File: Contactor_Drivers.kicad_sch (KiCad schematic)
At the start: 33 parts, among them Con1 LED, Con2 LED, Con3 LED, J4 Conn_01x04, J5 Conn_01x04, J6 Conn_01x04, J7 Conn_01x04, Q4 IRLML0030, Q5 IRLML0030, Q6 IRLML0030, U8 VOS618A

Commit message: changed some res values
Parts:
- R21, R23, R25: value 1k -> 2k
- R26: value R_US -> 1k
- U8: value VOS618A -> TCMT1106
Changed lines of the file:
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@@
 			)
 		)
-		(property "Value" "1k"
+		(property "Value" "2k"
 			(at 127 36.83 90)
 			(effects
@@
 			)
 		)
-		(property "Value" "R_US"
+		(property "Value" "1k"
 			(at 59.69 171.45 90)
 			(effects
@@
 			)
 		)
-		(property "Value" "1k"
+		(property "Value" "2k"
 			(at 57.15 36.83 90)
 			(effects
@@
 			)
 		)
-		(property "Value" "VOS618A"
+		(property "Value" "TCMT1106"
 			(at 77.47 171.45 0)
 			(effects
@@
 			)
 		)
-		(property "Value" "1k"
+		(property "Value" "2k"
 			(at 236.22 36.83 90)
 			(effects

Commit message: new revision for frank review
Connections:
- net M_Sense: no longer R26.1
- net MSense: now reaches C20.1, J6.2 (Pin_2), R32.2
- net MSense: now also R26.1
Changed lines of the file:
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@@
+	(wire
+		(pts
+			(xy 67.31 100.33) (xy 67.31 102.87)
+		)
+		(stroke
+			(width 0)
+			(type default)
+		)
+	)
 	(wire
 		(pts
@@
 	(wire
 		(pts
+			(xy 64.77 105.41) (xy 69.85 105.41)
+		)
+		(stroke
+			(width 0)
+			(type default)
+		)
+	)
+	(wire
+		(pts
 			(xy 241.3 102.87) (xy 248.92 102.87)
 		)
@@
 	(wire
 		(pts
+			(xy 44.45 175.26) (xy 55.88 175.26)
+		)
+		(stroke
+			(width 0)
+			(type default)
+		)
+	)
+	(wire
+		(pts
 			(xy 128.27 107.95) (xy 128.27 111.76)
 		)
@@
 	(wire
 		(pts
-			(xy 62.23 102.87) (xy 69.85 102.87)
+			(xy 62.23 100.33) (xy 67.31 100.33)
 		)
 		(stroke
@@
 	(wire
 		(pts
+			(xy 67.31 102.87) (xy 69.85 102.87)
+		)
+		(stroke
+			(width 0)
+			(type default)
+		)
+	)
+	(wire
+		(pts
 			(xy 219.71 107.95) (xy 222.25 107.95)
 		)
@@
 	(wire
 		(pts
-			(xy 48.26 175.26) (xy 55.88 175.26)
-		)
-		(stroke
-			(width 0)
-			(type default)
-		)
-	)
-	(wire
-		(pts
 			(xy 119.38 50.8) (xy 119.38 54.61)
 		)
@@
 	(wire
 		(pts
+			(xy 64.77 102.87) (xy 64.77 105.41)
+		)
+		(stroke
+			(width 0)
+			(type default)
+		)
+	)
+	(wire
+		(pts
 			(xy 66.04 71.12) (xy 66.04 77.47)
 		)
@@
 	(wire
 		(pts
-			(xy 69.85 105.41) (xy 62.23 105.41)
+			(xy 64.77 102.87) (xy 62.23 102.87)
 		)
 		(stroke
@@
 	(text "Motor\nCoil+"
 		(exclude_from_sim no)
-		(at 65.278 98.806 0)
+		(at 72.39 98.044 0)
 		(effects
 			(font
@@
 		)
 	)
+	(label "MSense"
+		(at 44.45 175.26 0)
+		(fields_autoplaced yes)
+		(effects
+			(font
+				(size 1.27 1.27)
+			)
+			(justify left bottom)
+		)
+	)
 	(label "MCon-"
 		(at 80.01 54.61 180)
@@
 			)
 			(justify right bottom)
+		)
+	)
+	(label "MSense"
+		(at 62.23 107.95 0)
+		(fields_autoplaced yes)
+		(effects
+			(font
+				(size 1.27 1.27)
+			)
+			(justify left bottom)
 		)
 	)
@@
 	(hierarchical_label "LV+"
 		(shape input)
-		(at 62.23 105.41 180)
+		(at 62.23 102.87 180)
 		(fields_autoplaced yes)
 		(effects
@@
 	(hierarchical_label "LV+"
 		(shape input)
-		(at 62.23 102.87 180)
+		(at 62.23 100.33 180)
 		(fields_autoplaced yes)
 		(effects
@@
 		)
 	)
-	(hierarchical_label "M_Sense"
-		(shape output)
-		(at 48.26 175.26 180)
-		(fields_autoplaced yes)
-		(effects
-			(font
-				(size 1.27 1.27)
-			)
-			(justify right)
-		)
-	)

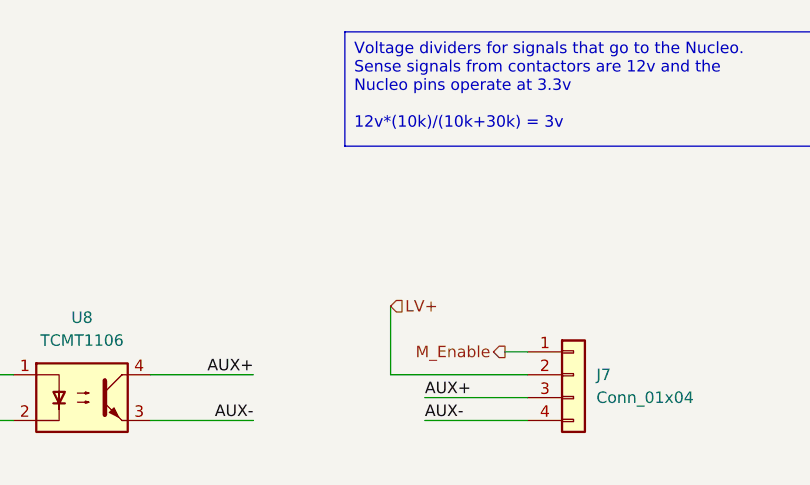
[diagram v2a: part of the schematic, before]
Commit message: emergency m_enable fix
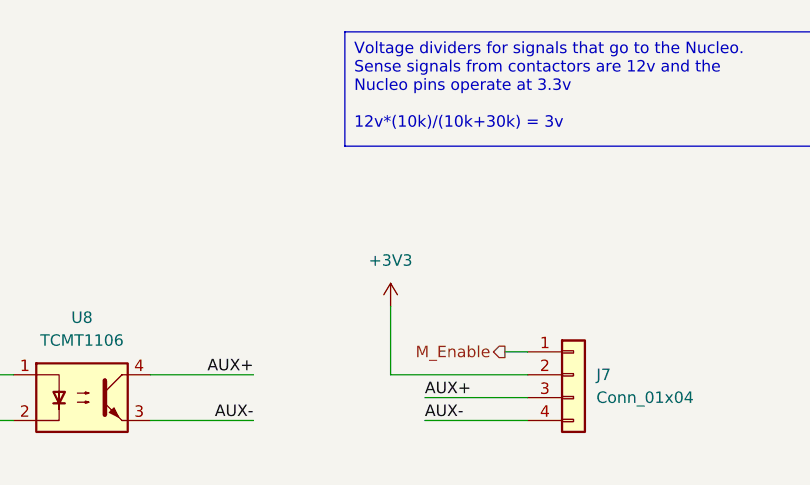
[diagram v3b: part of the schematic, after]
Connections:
- net LV+: no longer J7.2 (Pin_2)
- new net +3V3: J7.2 (Pin_2)
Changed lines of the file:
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@@
-		)
-	)
-	(hierarchical_label "LV+"
-		(shape input)
-		(at 111.76 167.64 0)
-		(fields_autoplaced yes)
-		(effects
-			(font
-				(size 1.27 1.27)
-			)
-			(justify left)
 		)
 	)
@@
 					(unit 1)
 				)
+			)
+		)
+	)
+	(symbol
+		(lib_id "power:+3V3")
+		(at 111.76 167.64 0)
+		(unit 1)
+		(exclude_from_sim no)
+		(in_bom yes)
+		(on_board yes)
+		(dnp no)
+		(fields_autoplaced yes)
+		(property "Reference" "#PWR018"
+			(at 111.76 171.45 0)
+			(effects
+				(font
+					(size 1.27 1.27)
+				)
+				(hide yes)
+			)
+		)
+		(property "Value" "+3V3"
+			(at 111.76 162.56 0)
+			(effects
+				(font
+					(size 1.27 1.27)
+				)
+			)
+		)
+		(property "Footprint" ""
+			(at 111.76 167.64 0)
+			(effects
+				(font
+					(size 1.27 1.27)
+				)
+				(hide yes)
+			)
+		)
+		(property "Datasheet" ""
+			(at 111.76 167.64 0)
+			(effects
+				(font
+					(size 1.27 1.27)
+				)
+				(hide yes)
+			)
+		)
+		(property "Description" "Power symbol creates a global label with name \"+3V3\""
+			(at 111.76 167.64 0)
+			(effects
+				(font
+					(size 1.27 1.27)
+				)
+				(hide yes)
+			)
+		)
+		(pin "1"
+		)
+		(instances
+			(project "ActivePrecharge"
+				(path "/b9847a31-2b3b-47ca-9561-fab506416f6d/c0036b4f-8078-47a1-85ab-72dbdcf28d35"
+					(reference "#PWR018")
+					(unit 1)
+				)
